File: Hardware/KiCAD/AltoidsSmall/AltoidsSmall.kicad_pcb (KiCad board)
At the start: 4 copper layers, 55 x 35 mm, 49 parts, among them J1 Conn_01x10_Male, J2 Conn_01x10_Male, J3 Conn_01x03_Male, J4 Conn_01x03_Male, J5 Conn_01x06_Male, SW1 SW_Push, SW2 SW_Push, U1 SC662K-3.3V, U2 STM32F103C8Tx, U3 FT230XQ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

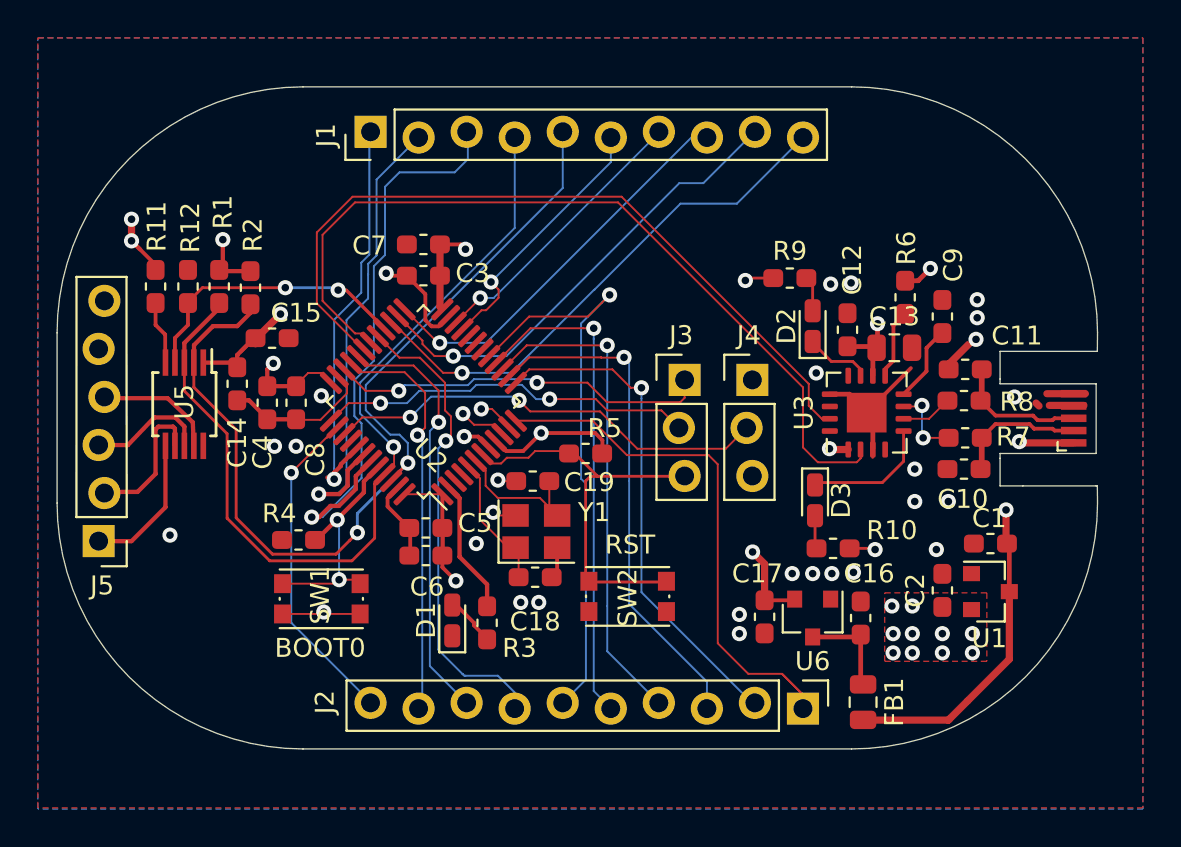
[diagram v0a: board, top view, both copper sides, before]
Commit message: Added labels to pins, Added part numbers
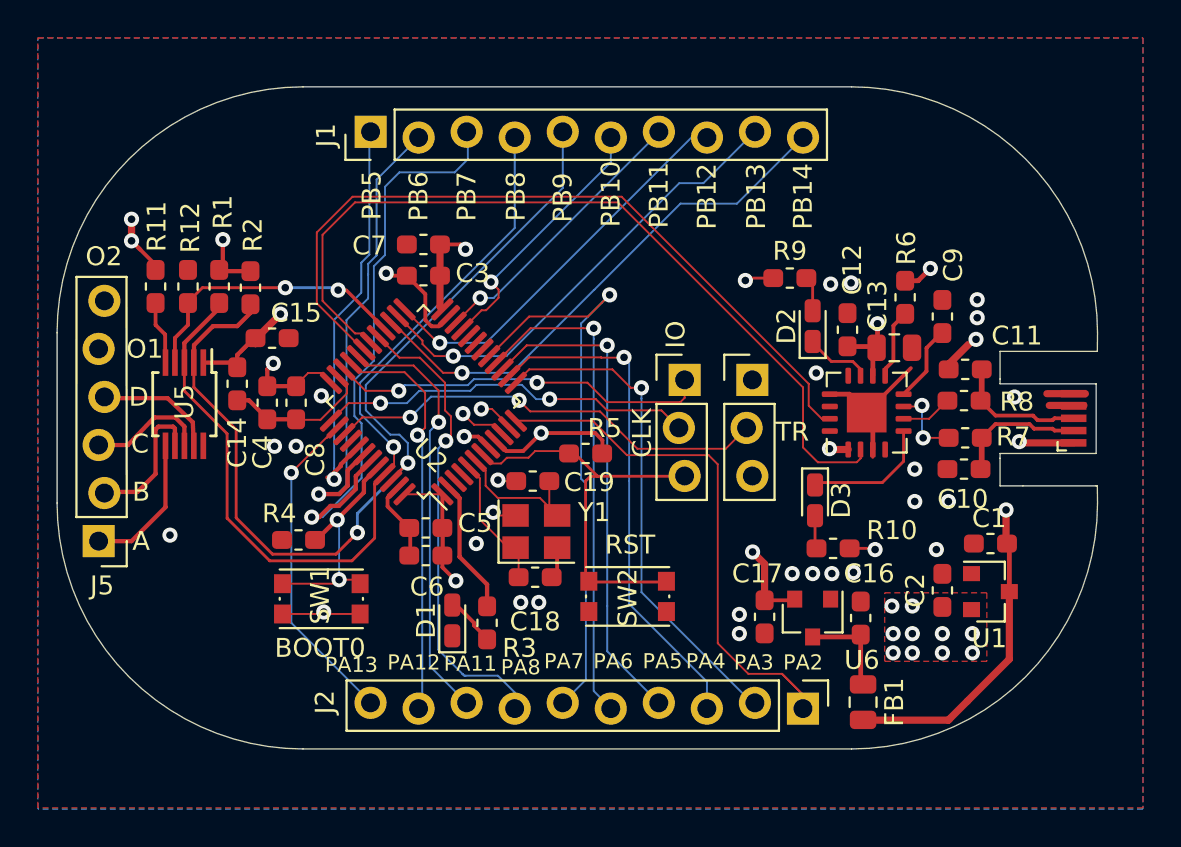
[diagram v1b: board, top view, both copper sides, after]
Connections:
- net Net-(J3-Pad1) renamed /MCU/SWDIO
- net Net-(J3-Pad2) renamed /MCU/SWCLK
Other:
- board text added: "A"
- board text added: "B"
- board text added: "C"
- board text added: "CLK"
- board text added: "D"
- board text added: "IO"
- board text added: "O1"
- board text added: "O2"
- board text added: "PA11"
- board text added: "PA12"
- board text added: "PA13"
- board text added: "PA2"
- board text added: "PA3"
- board text added: "PA4"
- board text added: "PA5"
- board text added: "PA6"
- board text added: "PA7"
- board text added: "PA8"
- board text added: "PB10"
- board text added: "PB11"
- board text added: "PB12"
- board text added: "PB13"
- board text added: "PB14"
- board text added: "PB5"
- board text added: "PB6"
- board text added: "PB7"
- board text added: "PB8"
- board text added: "PB9"
- board text added: "TR"
